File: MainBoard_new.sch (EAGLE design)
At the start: 60 parts, among them T1 BC847, U1 STM32F10XRXT6, Y1 8MHz, Y2 32.768kHz

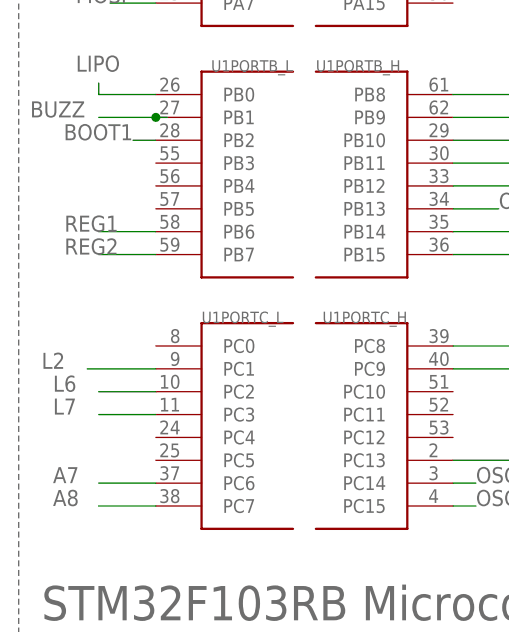
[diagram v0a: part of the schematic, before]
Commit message: zgubione sygnały przerwań
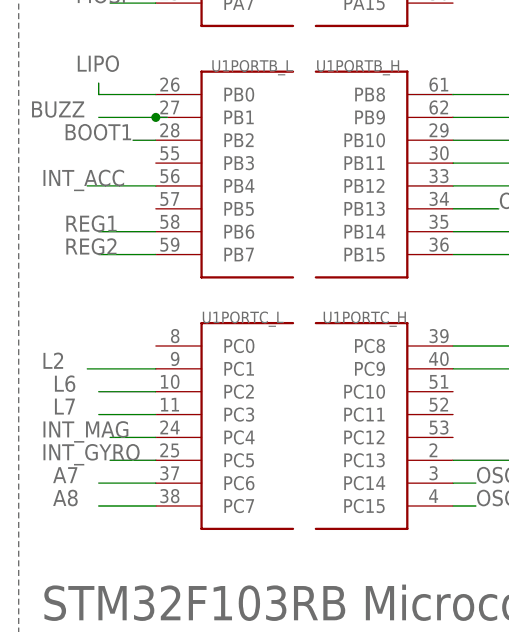
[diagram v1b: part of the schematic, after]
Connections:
- net INT_ACC: now also U1PORTB_L.PB4
- net INT_GYRO: now also U1PORTC_L.PC5
- net INT_MAG: now also U1PORTC_L.PC4
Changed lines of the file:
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@@
 <label x="200.66" y="22.86" size="1.778" layer="95"/>
+</segment>
+<segment>
+<pinref part="U1" gate="PORTC_L" pin="PC4"/>
+<wire x1="15.24" y1="22.86" x2="10.16" y2="22.86" width="0.1524" layer="91"/>
+<label x="2.54" y="22.86" size="1.778" layer="95"/>
 </segment>
 </net>
@@
 <label x="220.98" y="106.68" size="1.778" layer="95"/>
 </segment>
+<segment>
+<pinref part="U1" gate="PORTB_L" pin="PB4"/>
+<wire x1="15.24" y1="50.8" x2="7.62" y2="50.8" width="0.1524" layer="91"/>
+<label x="2.54" y="50.8" size="1.778" layer="95"/>
+</segment>
 </net>
 <net name="INT_GYRO" class="0">
@@
 <label x="220.98" y="86.36" size="1.778" layer="95"/>
 </segment>
+<segment>
+<pinref part="U1" gate="PORTC_L" pin="PC5"/>
+<wire x1="15.24" y1="20.32" x2="10.16" y2="20.32" width="0.1524" layer="91"/>
+<label x="2.54" y="20.32" size="1.778" layer="95"/>
+</segment>
 </net>
